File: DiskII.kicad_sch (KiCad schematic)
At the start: 35 parts, among them J1 Apple II Expansion Slot, J2 DRIVE 2, J3 DRIVE 1, Q1 2N3906, Q2 MPSU51, Q3 MPSU51

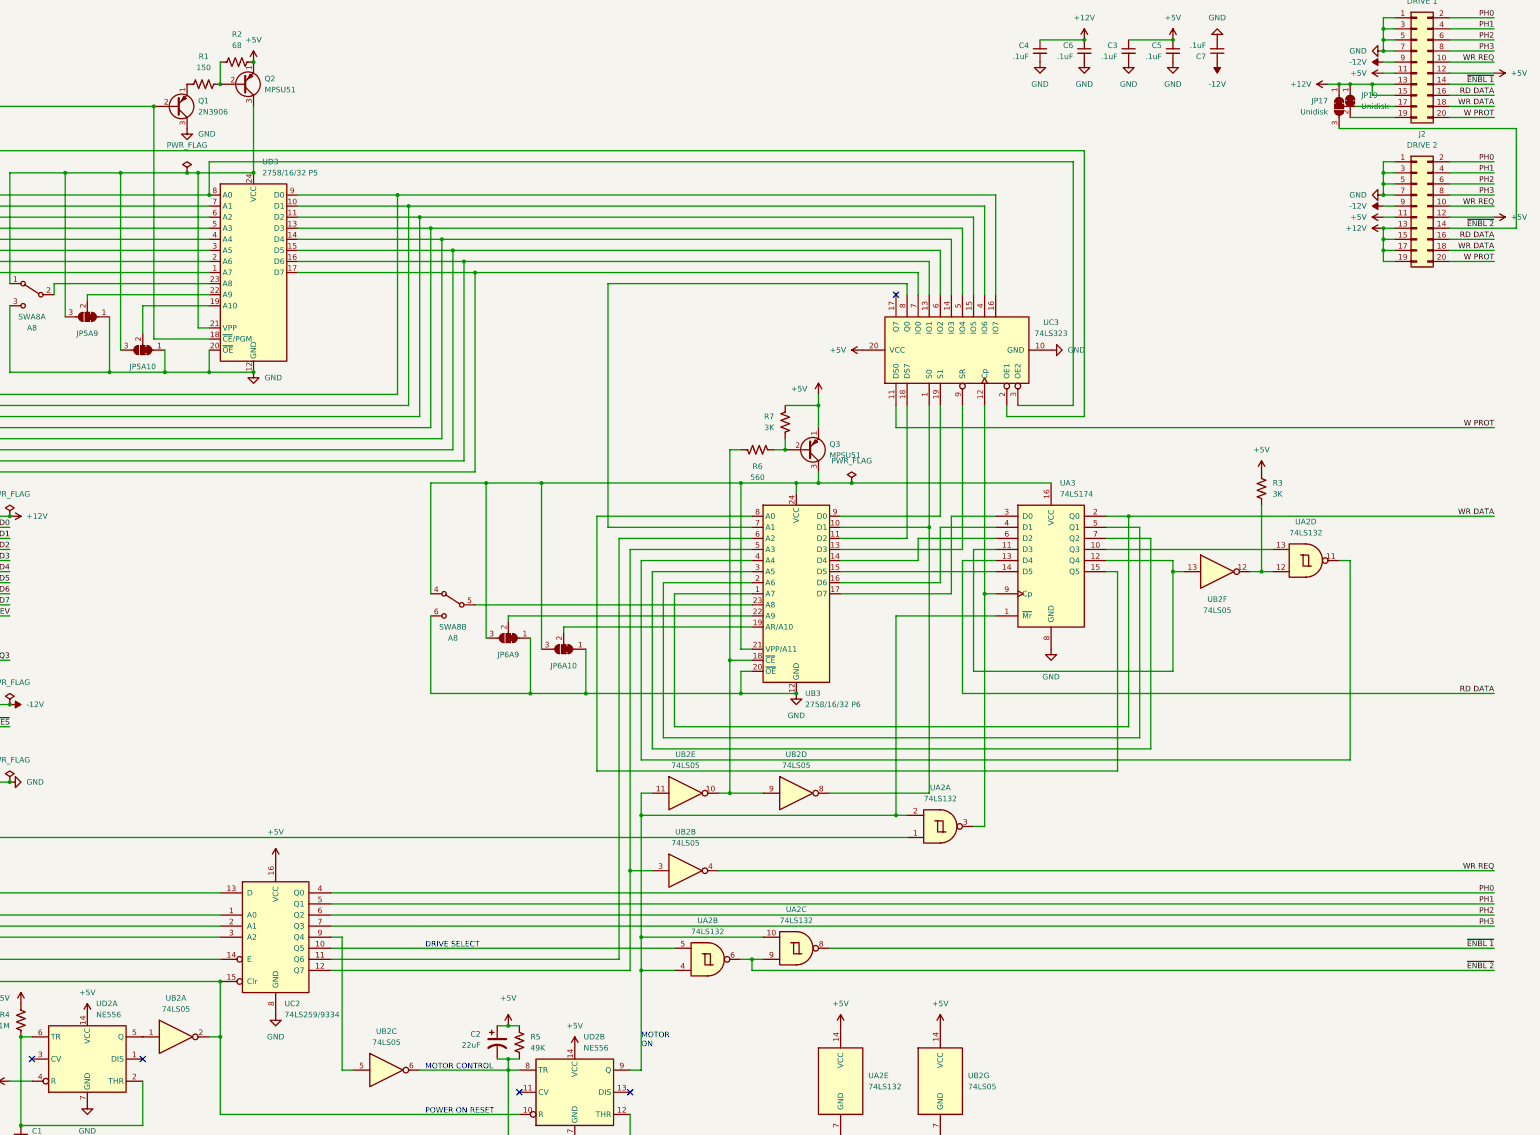
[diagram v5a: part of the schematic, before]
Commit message: jumper to put WPROT on pin 19
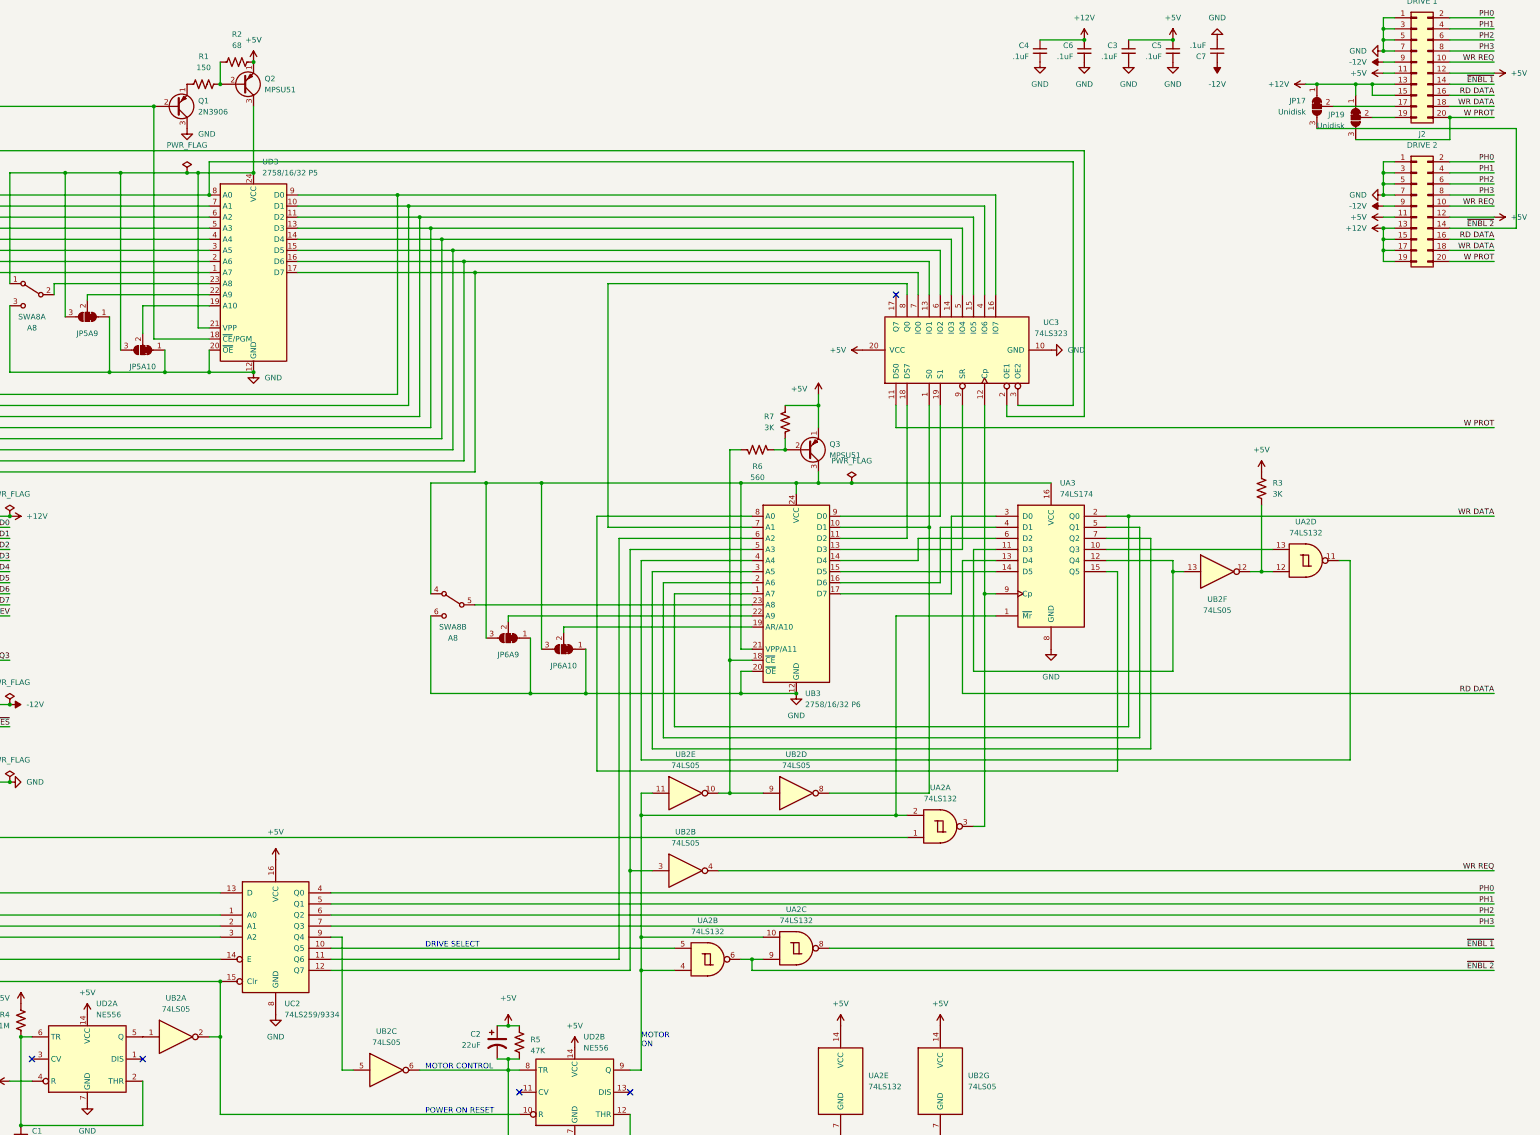
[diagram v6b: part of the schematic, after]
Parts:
- removed JP19: Unidisk, Jumper:SolderJumper-2_P1.3mm_Bridged_RoundedPad1.0x1.5mm, symbol Jumper:SolderJumper_2_Bridged
- added JP19: Unidisk, Jumper:SolderJumper-3_P1.3mm_Bridged12_RoundedPad1.0x1.5mm, symbol Jumper:SolderJumper_3_Bridged12
- R5: value 49K -> 47K
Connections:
- net +12V: now also JP19.1 (A)
- net W PROT: now also JP19.3 (B)
- net at J3.19 (Pin_19): now also JP19.2 (C)
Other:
- moved on the sheet: JP17

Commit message: starting rev 2
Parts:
- added R8: 470, Resistor_THT:R_Axial_DIN0207_L6.3mm_D2.5mm_P10.16mm_Horizontal, symbol Device:R_US
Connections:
- net GND: no longer J3.5 (Pin_5), J3.7 (Pin_7)
- net ~{ENBL 2}: now also R8.1
- new net: J3.5 (Pin_5), R8.2
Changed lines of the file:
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@@
   (paper "A3")
   (title_block
-    (rev "1")
+    (rev "2")
   )
   (junction (at 198.12 203.2) (diameter 0) (color 0 0 0 0)
@@
   (junction (at 309.88 134.62) (diameter 0) (color 0 0 0 0)
   )
-  (junction (at 368.3 25.4) (diameter 0) (color 0 0 0 0)
-  )
   (junction (at 53.34 195.58) (diameter 0) (color 0 0 0 0)
   )
@@
   (junction (at 368.3 73.66) (diameter 0) (color 0 0 0 0)
   )
+  (junction (at 353.06 45.72) (diameter 0) (color 0 0 0 0)
+  )
   (junction (at 86.36 40.64) (diameter 0) (color 0 0 0 0)
   )
@@
   (junction (at 55.88 254) (diameter 0) (color 0 0 0 0)
   )
-  (junction (at 368.3 22.86) (diameter 0) (color 0 0 0 0)
-  )
   (junction (at 231.14 119.38) (diameter 0) (color 0 0 0 0)
   )
-  (junction (at 368.3 27.94) (diameter 0) (color 0 0 0 0)
-  )
   (junction (at 142.24 60.96) (diameter 0) (color 0 0 0 0)
   )
@@
   )
   (junction (at 167.64 259.08) (diameter 0) (color 0 0 0 0)
+  )
+  (junction (at 368.3 20.32) (diameter 0) (color 0 0 0 0)
   )
   (junction (at 220.98 175.26) (diameter 0) (color 0 0 0 0)
@@
     (stroke (width 0) (type default))
   )
+  (wire (pts (xy 345.44 25.4) (xy 351.79 25.4))
+    (stroke (width 0) (type default))
+  )
   (wire (pts (xy 162.56 127) (xy 175.26 127))
     (stroke (width 0) (type default))
@@
     (stroke (width 0) (type default))
   )
-  (wire (pts (xy 368.3 22.86) (xy 368.3 25.4))
-    (stroke (width 0) (type default))
-  )
   (wire (pts (xy 256.54 203.2) (xy 259.08 203.2))
     (stroke (width 0) (type default))
@@
     (stroke (width 0) (type default))
   )
-  (wire (pts (xy 368.3 25.4) (xy 370.84 25.4))
-    (stroke (width 0) (type default))
-  )
   (wire (pts (xy 45.72 195.58) (xy 53.34 195.58))
     (stroke (width 0) (type default))
@@
     (stroke (width 0) (type default))
   )
+  (wire (pts (xy 353.06 45.72) (xy 345.44 45.72))
+    (stroke (width 0) (type default))
+  )
   (wire (pts (xy 203.2 149.86) (xy 223.52 149.86))
     (stroke (width 0) (type default))
@@
     (stroke (width 0) (type default))
   )
+  (wire (pts (xy 345.44 45.72) (xy 345.44 25.4))
+    (stroke (width 0) (type default))
+  )
   (wire (pts (xy 322.58 147.32) (xy 320.04 147.32))
     (stroke (width 0) (type default))
@@
     (stroke (width 0) (type default))
   )
-  (wire (pts (xy 368.3 25.4) (xy 368.3 27.94))
-    (stroke (width 0) (type default))
-  )
   (wire (pts (xy 63.5 81.28) (xy 99.06 81.28))
     (stroke (width 0) (type default))
@@
   )
   (wire (pts (xy 167.64 157.48) (xy 167.64 158.75))
+    (stroke (width 0) (type default))
+  )
+  (wire (pts (xy 359.41 25.4) (xy 370.84 25.4))
     (stroke (width 0) (type default))
   )
@@
     )
   )
-  (symbol (lib_id "power:GND") (at 368.3 27.94 270) (unit 1)
+  (symbol (lib_id "power:GND") (at 368.3 20.32 270) (unit 1)
     (in_bom yes) (on_board yes) (dnp no) (fields_autoplaced)
-    (property "Reference" "#PWR0130" (at 361.95 27.94 0)
-      (effects (font (size 1.27 1.27)) hide)
-    )
-    (property "Value" "GND" (at 364.49 27.9399 90)
+    (property "Reference" "#PWR0130" (at 361.95 20.32 0)
+      (effects (font (size 1.27 1.27)) hide)
+    )
+    (property "Value" "GND" (at 364.49 20.3199 90)
       (effects (font (size 1.27 1.27)) (justify right))
     )
-    (property "Footprint" "" (at 368.3 27.94 0)
-      (effects (font (size 1.27 1.27)) hide)
-    )
-    (property "Datasheet" "" (at 368.3 27.94 0)
+    (property "Footprint" "" (at 368.3 20.32 0)
+      (effects (font (size 1.27 1.27)) hide)
+    )
+    (property "Datasheet" "" (at 368.3 20.32 0)
       (effects (font (size 1.27 1.27)) hide)
     )
@@
         )
       )
+    )
+  )
+  (symbol (lib_id "Device:R_US") (at 355.6 25.4 90) (unit 1)
+    (in_bom yes) (on_board yes) (dnp yes) (fields_autoplaced)
+    (property "Reference" "R8" (at 355.6 20.32 90)
+      (effects (font (size 1.27 1.27)))
+    )
+    (property "Value" "470" (at 355.6 22.86 90)
+      (effects (font (size 1.27 1.27)))
+    )
+    (property "Footprint" "Resistor_THT:R_Axial_DIN0207_L6.3mm_D2.5mm_P10.16mm_Horizontal" (at 355.854 24.384 90)
+      (effects (font (size 1.27 1.27)) hide)
+    )
+    (property "Datasheet" "~" (at 355.6 25.4 0)
+      (effects (font (size 1.27 1.27)) hide)
+    )
+    (pin "1")
+    (pin "2")
+    (instances
+      (project "DiskII"
+        (path "/c5fa29fb-f00a-43d2-879f-1e361b003a2a"
+          (reference "R8") (unit 1)
+        )
+      )
